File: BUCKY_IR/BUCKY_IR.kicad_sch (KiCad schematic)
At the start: 18 parts

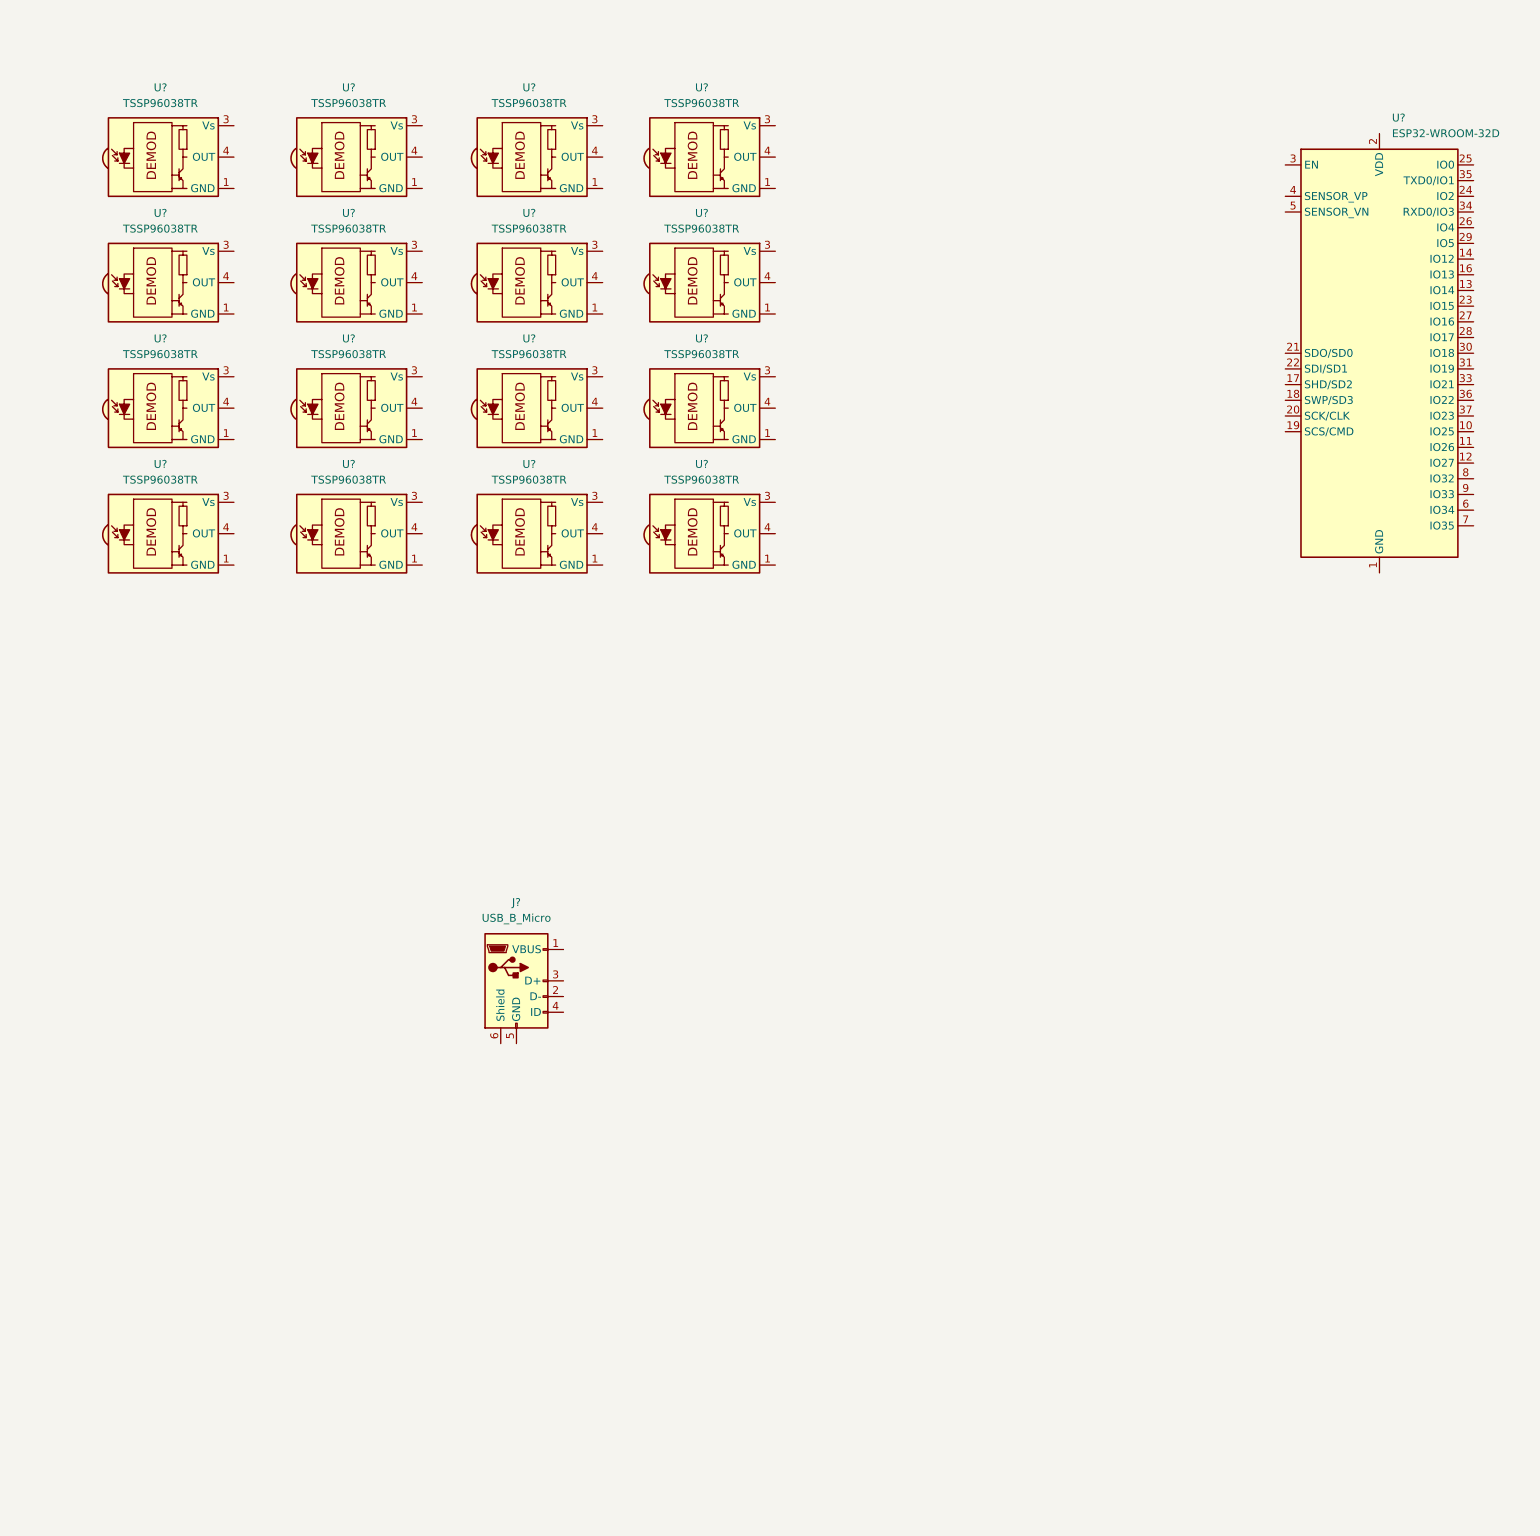
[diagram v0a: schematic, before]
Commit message: Finished up IR sch, Main, Started Power
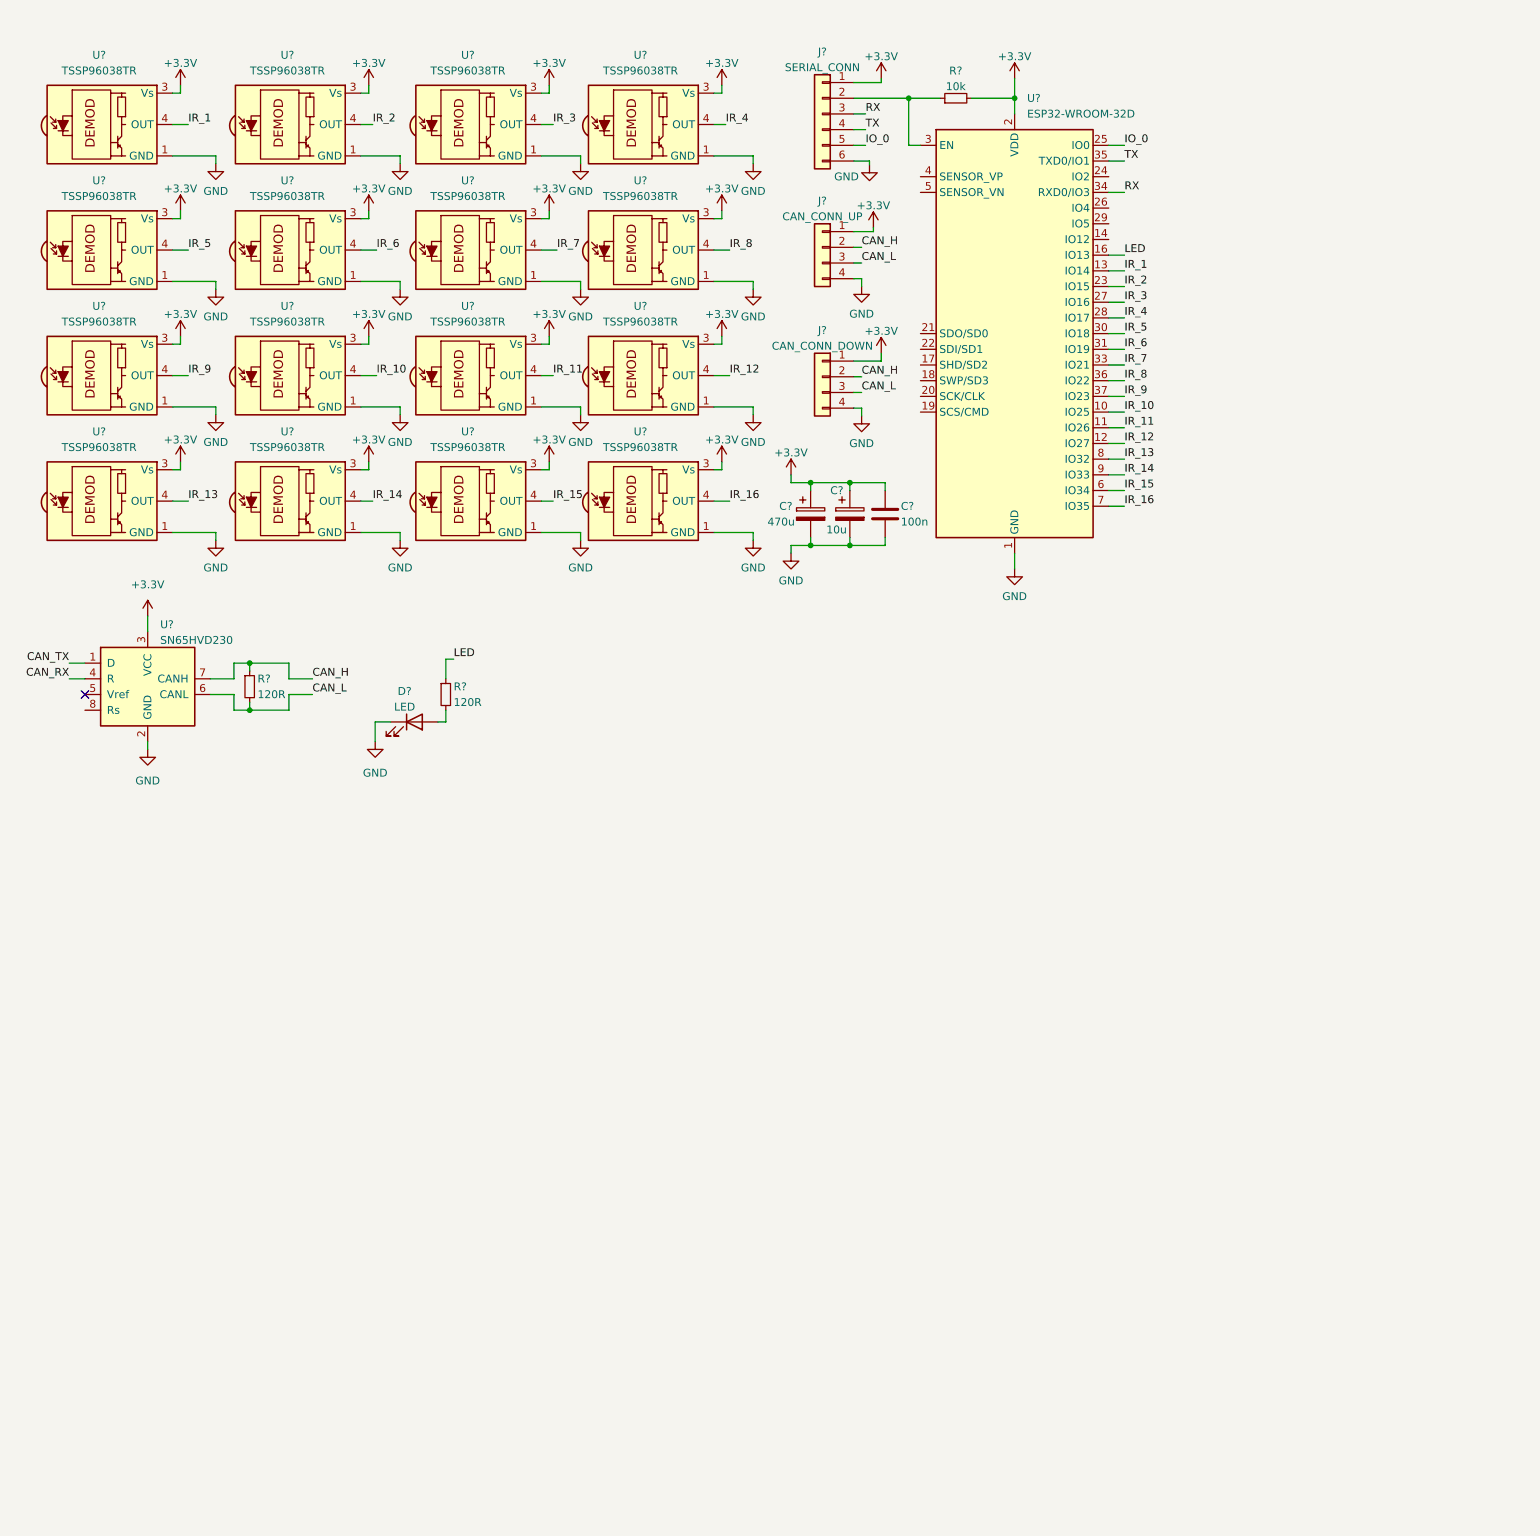
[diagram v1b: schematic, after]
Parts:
- removed J?: USB_B_Micro, symbol Connector:USB_B_Micro
- added C?: 470u, symbol Device:C_Polarized
- added C?: 10u, symbol Device:C_Polarized
- added C?: 100n, symbol Device:C
- added D?: LED, symbol Device:LED
- added J?: SERIAL_CONN, symbol Connector_Generic:Conn_01x06
- added J?: CAN_CONN_DOWN, symbol Connector_Generic:Conn_01x04
- added J?: CAN_CONN_UP, symbol Connector_Generic:Conn_01x04
- added R? (x2): 120R, symbol Device:R_Small
- added R?: 10k, symbol Device:R_Small
- added U?: SN65HVD230, Package_SO:SOIC-8_3.9x4.9mm_P1.27mm, symbol Interface_CAN_LIN:SN65HVD230
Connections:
- net GND: now reaches U?.1 (GND)
- net GND: now also U?.1 (GND), U?.1 (GND), U?.1 (GND), U?.1 (GND), U?.1 (GND), U?.1 (GND), U?.1 (GND), U?.1 (GND), U?.1 (GND), U?.1 (GND), U?.1 (GND), U?.1 (GND), U?.1 (GND), U?.1 (GND), U?.1 (GND), U?.1 (GND), U?.15 (GND), U?.38 (GND), U?.39 (GND), C?.2, C?.2, C?.2, D?.1 (K), J?.4 (Pin_4), J?.4 (Pin_4), J?.6 (Pin_6), U?.2 (GND)
- net +3V3: now reaches U?.3 (Vs)
- net +3V3: now also U?.2 (VDD), U?.3 (Vs), U?.3 (Vs), U?.3 (Vs), U?.3 (Vs), U?.3 (Vs), U?.3 (Vs), U?.3 (Vs), U?.3 (Vs), U?.3 (Vs), U?.3 (Vs), U?.3 (Vs), U?.3 (Vs), U?.3 (Vs), U?.3 (Vs), U?.3 (Vs), C?.1, C?.1, C?.1, J?.1 (Pin_1), J?.1 (Pin_1), J?.1 (Pin_1), R?.2, U?.3 (VCC)
- net IR_1: now reaches U?.4 (OUT)
- net IR_1: now also U?.13 (IO14)
- net IR_12: now reaches U?.4 (OUT)
- net IR_12: now also U?.12 (IO27)
- net IR_3: now reaches U?.4 (OUT)
- net IR_3: now also U?.27 (IO16)
- net IR_9: now reaches U?.4 (OUT)
- net IR_9: now also U?.37 (IO23)
- net IR_5: now reaches U?.4 (OUT)
- net IR_5: now also U?.30 (IO18)
- net IR_14: now reaches U?.4 (OUT)
- net IR_14: now also U?.9 (IO33)
- net IR_8: now reaches U?.4 (OUT)
- net IR_8: now also U?.36 (IO22)
- net IR_11: now reaches U?.4 (OUT)
- net IR_11: now also U?.11 (IO26)
- net IR_16: now reaches U?.4 (OUT)
- net IR_16: now also U?.7 (IO35)
- net IR_15: now reaches U?.4 (OUT)
- net IR_15: now also U?.6 (IO34)
- net IR_13: now reaches U?.4 (OUT)
- net IR_13: now also U?.8 (IO32)
- net IR_10: now reaches U?.4 (OUT)
- net IR_10: now also U?.10 (IO25)
- net IR_4: now reaches U?.4 (OUT)
- net IR_4: now also U?.28 (IO17)
- net IR_6: now reaches U?.4 (OUT)
- net IR_6: now also U?.31 (IO19)
- net IR_2: now reaches U?.4 (OUT)
- net IR_2: now also U?.23 (IO15)
- net LED: now reaches U?.16 (IO13)
- net LED: now also R?.1
- net IO_0: now reaches U?.25 (IO0)
- net IO_0: now also J?.5 (Pin_5)
- net at U?.3 (EN): now also J?.2 (Pin_2), R?.1
- net IR_7: now reaches U?.33 (IO21)
- net IR_7: now also U?.4 (OUT)
- net RX: now reaches U?.34 (RXD0/IO3)
- net RX: now also J?.3 (Pin_3)
- net TX: now reaches U?.35 (TXD0/IO1)
- net TX: now also J?.4 (Pin_4)
- new net: D?.2 (A), R?.2
- new net CAN_H: J?.2 (Pin_2), J?.2 (Pin_2), R?.1, U?.7 (CANH)
- new net CAN_L: J?.3 (Pin_3), J?.3 (Pin_3), R?.2, U?.6 (CANL)
- new net CAN_RX: U?.4 (R)
- new net CAN_TX: U?.1 (D)
- no-connect marks 0 -> 1
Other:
- moved on the sheet: U?

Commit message: Started IR PCB
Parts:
- C1, C2: renamed from C?; footprint (none) -> Capacitor_SMD:CP_Elec_6.3x7.7
- C3: renamed from C?; footprint (none) -> Capacitor_SMD:C_0805_2012Metric_Pad1.18x1.45mm_HandSolder
- D1: renamed from D?; footprint (none) -> LED_SMD:LED_0805_2012Metric_Pad1.15x1.40mm_HandSolder
- J1, J2, J3: renamed from J?; footprint (none) -> Connector_JST:JST_PH_B6B-PH-K_1x06_P2.00mm_Vertical
- R1, R2, R3: renamed from R?; footprint (none) -> Resistor_SMD:R_0805_2012Metric_Pad1.20x1.40mm_HandSolder
- gave numbers to parts that had none: 18
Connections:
- net CAN_RX: now also U18.26 (IO4)
- net CAN_TX: now also U18.29 (IO5)

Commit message: Started Light PCB
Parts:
- added U19: AMS1117, Package_TO_SOT_SMD:SOT-223-3_TabPin2, symbol Regulator_Linear:AMS1117
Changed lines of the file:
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@@
     (pin "1")
+  )
+  (symbol (lib_id "Regulator_Linear:AMS1117") (at 189.865 15.24 0) (unit 1)
+    (in_bom yes) (on_board yes) (fields_autoplaced)
+    (property "Reference" "U19" (id 0) (at 189.865 9.6352 0))
+    (property "Value" "AMS1117" (id 1) (at 189.865 12.1721 0))
+    (property "Footprint" "Package_TO_SOT_SMD:SOT-223-3_TabPin2" (id 2) (at 189.865 10.16 0)
+      (effects (font (size 1.27 1.27)) hide)
+    )
+    (property "Datasheet" "http://www.advanced-monolithic.com/pdf/ds1117.pdf" (id 3) (at 192.405 21.59 0)
+      (effects (font (size 1.27 1.27)) hide)
+    )
+    (pin "1")
+    (pin "2")
+    (pin "3")
   )
   (symbol (lib_id "power:GND") (at 131.0391 73.4695 0) (unit 1)
@@
       (reference "U18") (unit 1) (value "ESP32-WROOM-32D") (footprint "RF_Module:ESP32-WROOM-32")
     )
-  )
+    (path "/c704b6f6-f527-4c2e-9d83-ff759777f370"
+      (reference "U19") (unit 1) (value "AMS1117") (footprint "Package_TO_SOT_SMD:SOT-223-3_TabPin2")
+    )
+  )

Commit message: Some IR changes
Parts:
- renumbered U8 to U10, U12 to U11, U16 to U12, U4 to U13, U9 to U14, U13 to U15, U17 to U16, U5 to U17, U6 to U2, U10 to U3, U14 to U4, U2 to U5, U7 to U6, U11 to U7, U15 to U8, U3 to U9

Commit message: More IR dev
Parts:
- removed J2: CAN_CONN_UP, Connector_JST:JST_PH_B6B-PH-K_1x06_P2.00mm_Vertical, symbol Connector_Generic:Conn_01x04
- removed J3: CAN_CONN_DOWN, Connector_JST:JST_PH_B6B-PH-K_1x06_P2.00mm_Vertical, symbol Connector_Generic:Conn_01x04
- removed U19: AMS1117, Package_TO_SOT_SMD:SOT-223-3_TabPin2, symbol Regulator_Linear:AMS1117
- added C4: 10u, Capacitor_SMD:CP_Elec_6.3x7.7, symbol Device:C_Polarized
- added C5: 100n, Capacitor_SMD:C_0805_2012Metric_Pad1.18x1.45mm_HandSolder, symbol Device:C
- added J2: CAN_CONN_UP, Connector_JST:JST_PH_S6B-PH-SM4-TB_1x06-1MP_P2.00mm_Horizontal, symbol Connector_Generic:Conn_01x06
- added J3: CAN_CONN_DOWN, Connector_JST:JST_PH_S6B-PH-SM4-TB_1x06-1MP_P2.00mm_Horizontal, symbol Connector_Generic:Conn_01x06
- added U19: AMS1117-5.0, Package_TO_SOT_SMD:SOT-223-3_TabPin2, symbol Regulator_Linear:AMS1117-5.0
- J1: footprint Connector_JST:JST_PH_B6B-PH-K_1x06_P2.00mm_Vertical -> Connector_JST:JST_PH_S6B-PH-SM4-TB_1x06-1MP_P2.00mm_Horizontal
- U18: value ESP32-WROOM-32D -> ESP32-WROOM-32U; footprint RF_Module:ESP32-WROOM-32 -> RF_Module:ESP32-WROOM-32U; symbol RF_Module:ESP32-WROOM-32D -> RF_Module:ESP32-WROOM-32U
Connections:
- net +3V3: now also C4.1, C5.1, J2.3 (Pin_3), J3.3 (Pin_3), U19.2 (VO); no longer C1.1, C2.1, C3.1
- net CAN_H: now also J2.4 (Pin_4), J3.4 (Pin_4)
- net CAN_L: now also J2.5 (Pin_5), J3.5 (Pin_5)
- net GND: now also C4.2, C5.2, J2.6 (Pin_6), J3.6 (Pin_6), U19.1 (GND)
- net IR_10: now also U18.36 (IO22); no longer U18.10 (IO25)
- net IR_11: now also U18.33 (IO21); no longer U18.11 (IO26)
- net IR_12: now also U18.31 (IO19); no longer U18.12 (IO27)
- net IR_13: now also U18.30 (IO18); no longer U18.8 (IO32)
- net IR_14: now also U18.28 (IO17); no longer U18.9 (IO33)
- net IR_15: now also U18.27 (IO16); no longer U18.6 (IO34)
- net IR_16: now also U18.23 (IO15); no longer U18.7 (IO35)
- net IR_2: now also U18.12 (IO27); no longer U18.23 (IO15)
- net IR_3: now also U18.11 (IO26); no longer U18.27 (IO16)
- net IR_4: now also U18.10 (IO25); no longer U18.28 (IO17)
- net IR_5: now also U18.9 (IO33); no longer U18.30 (IO18)
- net IR_6: now also U18.8 (IO32); no longer U18.31 (IO19)
- net IR_7: now also U18.7 (IO35); no longer U18.33 (IO21)
- net IR_8: now also U18.6 (IO34); no longer U18.36 (IO22)
- new net +5V: C1.1, C2.1, C3.1, J2.1 (Pin_1), J2.2 (Pin_2), J3.1 (Pin_1), J3.2 (Pin_2), U19.3 (VI)
- no-connect marks 1 -> 9
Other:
- moved on the sheet: C1, C2, C3, D1, J1, R2, R3, U18

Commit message: Finished PCBS
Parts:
- added J4: PHOTODIODE, Connector_PinHeader_2.54mm:PinHeader_1x02_P2.54mm_Horizontal, symbol Connector_Generic:Conn_01x02
- added J5: LED, Connector_PinHeader_2.54mm:PinHeader_1x02_P2.54mm_Horizontal, symbol Connector_Generic:Conn_01x02
- added R4: 10k, Resistor_SMD:R_0805_2012Metric_Pad1.20x1.40mm_HandSolder, symbol Device:R_Small
- added R5: 120R, Resistor_SMD:R_0805_2012Metric_Pad1.20x1.40mm_HandSolder, symbol Device:R_Small
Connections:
- net +3V3: now also R4.1, R5.1
- net GND: now also J4.2 (Pin_2), J5.2 (Pin_2)
- net PD: now reaches U18.14 (IO12)
- net PD: now also J4.1 (Pin_1), R4.2
- new net: J5.1 (Pin_1), R5.2

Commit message: chore: start on schematics
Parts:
- removed C1: 470u, Capacitor_SMD:CP_Elec_6.3x7.7, symbol Device:C_Polarized
- removed C2, C4: 10u, Capacitor_SMD:CP_Elec_6.3x7.7, symbol Device:C_Polarized
- removed D1: LED, LED_SMD:LED_0805_2012Metric_Pad1.15x1.40mm_HandSolder, symbol Device:LED
- removed J1: SERIAL_CONN, Connector_JST:JST_PH_S6B-PH-SM4-TB_1x06-1MP_P2.00mm_Horizontal, symbol Connector_Generic:Conn_01x06
- removed J2: CAN_CONN_UP, Connector_JST:JST_PH_S6B-PH-SM4-TB_1x06-1MP_P2.00mm_Horizontal, symbol Connector_Generic:Conn_01x06
- removed J3: CAN_CONN_DOWN, Connector_JST:JST_PH_S6B-PH-SM4-TB_1x06-1MP_P2.00mm_Horizontal, symbol Connector_Generic:Conn_01x06
- removed J4: PHOTODIODE, Connector_PinHeader_2.54mm:PinHeader_1x02_P2.54mm_Horizontal, symbol Connector_Generic:Conn_01x02
- removed J5: LED, Connector_PinHeader_2.54mm:PinHeader_1x02_P2.54mm_Horizontal, symbol Connector_Generic:Conn_01x02
- removed R1, R2, R5: 120R, Resistor_SMD:R_0805_2012Metric_Pad1.20x1.40mm_HandSolder, symbol Device:R_Small
- removed R3, R4: 10k, Resistor_SMD:R_0805_2012Metric_Pad1.20x1.40mm_HandSolder, symbol Device:R_Small
- removed U1, U10, U11, U12, U13, U14, U15, U16, U2, U3, U4, U5, U6, U7, U8, U9: TSSP96038TR, BUCKY_IR:TSSP96038, symbol BUCKY_IR:TSSP96038TR
- removed U17: SN65HVD230, Package_SO:SOIC-8_3.9x4.9mm_P1.27mm, symbol Interface_CAN_LIN:SN65HVD230
- removed U18: ESP32-WROOM-32U, RF_Module:ESP32-WROOM-32U, symbol RF_Module:ESP32-WROOM-32U
- removed U19: AMS1117-5.0, Package_TO_SOT_SMD:SOT-223-3_TabPin2, symbol Regulator_Linear:AMS1117-5.0
- added A1: Arduino_Mega2560_R3_Shield, PCM_arduino-library:Arduino_Mega2560_R3_Shield, symbol PCM_arduino-library:Arduino_Mega2560_R3_Shield
- added C1, C10, C11, C12, C2, C4, C6, C7, C8, C9: 10uF, symbol Device:C
- added D1, D10, D11, D12, D13, D15, D2, D3, D4, D5, D6, D7, D8, D9: D, symbol Device:D
- added IC1, IC10, IC11, IC12, IC2, IC3, IC4, IC5, IC6, IC7, IC8, IC9: TSSP96038TR, TSSP96038TR, symbol BUCKY_IR:TSSP96038TR
- added J1: Conn_01x10, BUCKY_MAIN:CONN10_S10B-PH_JST, symbol Connector_Generic:Conn_01x10
- added J2: Conn_01x16, symbol Connector_Generic:Conn_01x16
- added J3: Conn_01x02, symbol Connector_Generic:Conn_01x02
- C3, C5: value 100n -> 10uF; footprint Capacitor_SMD:C_0805_2012Metric_Pad1.18x1.45mm_HandSolder -> (none)
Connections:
- net +3V3 is gone; now on net GND: C5.1
- net +5V: now also A1.5V1 (5V), A1.5V3 (5V), A1.5V4 (5V), A1.AREF, D1.2 (A), D10.2 (A), D11.2 (A), D12.2 (A), D13.1 (K), D2.2 (A), D3.2 (A), D4.2 (A), D5.2 (A), D6.2 (A), D7.2 (A), D8.2 (A), D9.2 (A); no longer C3.1
- net GND: now also C3.1, A1.GND1 (GND), A1.GND2 (GND), A1.GND3 (GND), A1.GND5 (GND), A1.GND6 (GND), C1.1, C10.1, C11.1, C12.1, C2.1, C4.1, C6.1, C7.1, C8.1, C9.1, IC1.1 (GND), IC10.1 (GND), IC11.1 (GND), IC12.1 (GND), IC2.1 (GND), IC3.1 (GND), IC4.1 (GND), IC5.1 (GND), IC6.1 (GND), IC7.1 (GND), IC8.1 (GND), IC9.1 (GND), J1.10 (Pin_10), J3.2 (Pin_2); no longer C3.2, C5.2
- net IR_1: now also A1.D22, IC1.4 (OUT)
- net IR_10: now also A1.D31, IC10.4 (OUT)
- net IR_11: now also A1.D32, IC11.4 (OUT)
- net IR_12: now also A1.D33, IC12.4 (OUT)
- net IR_2: now also A1.D23, IC2.4 (OUT)
- net IR_3: now also A1.D24, IC3.4 (OUT)
- net IR_4: now also A1.D25, IC4.4 (OUT)
- net IR_5: now also A1.D26, IC5.4 (OUT)
- net IR_6: now also A1.D27, IC6.4 (OUT)
- net IR_7: now also A1.D28, IC7.4 (OUT)
- net IR_8: now also A1.D29, IC8.4 (OUT)
- net IR_9: now also A1.D30, IC9.4 (OUT)
- new net: D15.1 (K), J3.1 (Pin_1)
- new net: C3.2, D3.1 (K), IC3.3 (VS)
- new net: C8.2, D8.1 (K), IC8.3 (VS)
- new net: C4.2, D4.1 (K), IC4.3 (VS)
- new net: C10.2, D11.1 (K), IC10.3 (VS)
- new net: C2.2, D2.1 (K), IC2.3 (VS)
- new net: C11.2, D10.1 (K), IC11.3 (VS)
- new net: C6.2, D6.1 (K), IC6.3 (VS)
- new net: C9.2, D12.1 (K), IC9.3 (VS)
- new net: C5.2, D5.1 (K), IC5.3 (VS)
- new net: C7.2, D7.1 (K), IC7.3 (VS)
- new net: C1.2, D1.1 (K), IC1.3 (VS)
- new net: C12.2, D9.1 (K), IC12.3 (VS)
- new net +3.3V: A1.3V3 (3.3V)
- new net D_A: A1.A0, J2.1 (Pin_1)
- new net D_S0: A1.D42, J2.10 (Pin_10)
- new net D_S1: A1.D47, J2.15 (Pin_15)
- new net D_S2: A1.D41, J2.9 (Pin_9)
- new net F_A: A1.A3, J2.4 (Pin_4)
- new net F_S0: A1.D38, J2.6 (Pin_6)
- new net F_S1: A1.D39, J2.7 (Pin_7)
- new net F_S2: A1.D40, J2.8 (Pin_8)
- new net L_A: A1.A1, J2.2 (Pin_2)
- new net L_S0: A1.D48, J2.16 (Pin_16)
- new net L_S1: A1.D46, J2.14 (Pin_14)
- new net L_S2: A1.D37, J2.5 (Pin_5)
- new net M1_DIR: A1.D34, J1.4 (Pin_4)
- new net M1_PWM: A1.D11, J1.3 (Pin_3)
- new net M2_DIR: A1.D35, J1.2 (Pin_2)
- new net M2_PWM: A1.D12, J1.1 (Pin_1)
- new net M3_DIR: A1.D36, J1.6 (Pin_6)
- new net M3_PWM: A1.D13, J1.5 (Pin_5)
- new net R_A: A1.A2, J2.3 (Pin_3)
- new net R_S0: A1.D45, J2.13 (Pin_13)
- new net R_S1: A1.D44, J2.12 (Pin_12)
- new net R_S2: A1.D43, J2.11 (Pin_11)
- new net SCL: A1.SCL, J1.8 (Pin_8)
- new net SDA: A1.SDA, J1.7 (Pin_7)
- new net VIN: A1.VIN, D13.2 (A), D15.2 (A), J1.9 (Pin_9)
- no-connect marks 9 -> 10
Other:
- note added: "BUCKY LIGHT"
- note added: "BUCKY LIGHT POWER"
- note added: "BUCKY MAIN"
- note added: "CONNECTORS"
- note added: "INFRARED SENSORS"
- note added: "MCU (ARDUINO MEGA R3)"
- note added: "THE DIODES ARE TO MAKE PROBING EASIER"
- company: (none) -> koen1711
- title: (none) -> BUCKY IR
